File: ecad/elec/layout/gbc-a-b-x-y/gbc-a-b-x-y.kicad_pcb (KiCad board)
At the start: 2 copper layers, 225.7 x 100.8 mm, 0 parts

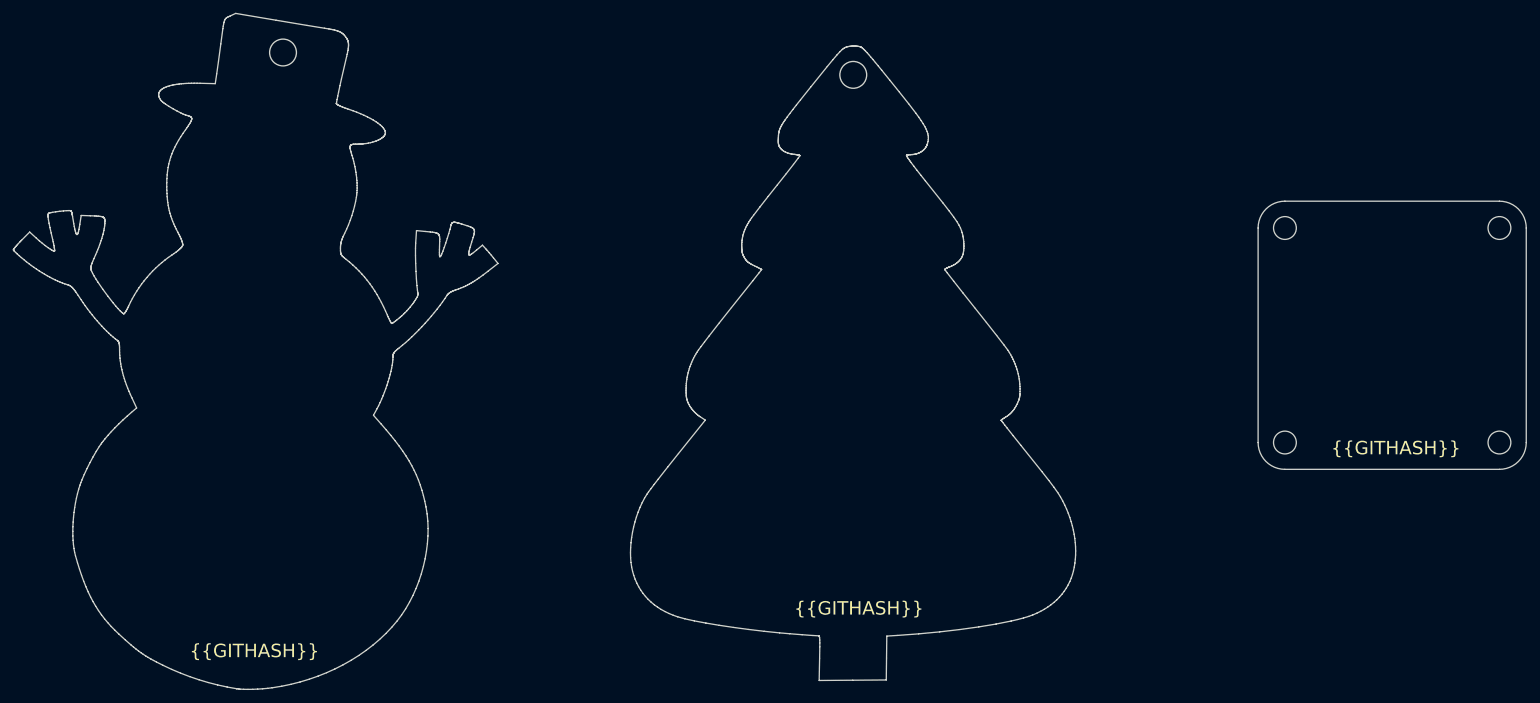
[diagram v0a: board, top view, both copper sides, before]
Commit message: WIP fleshing out and redoing some of the design to add some footprints / components for slik / membranes / etc.
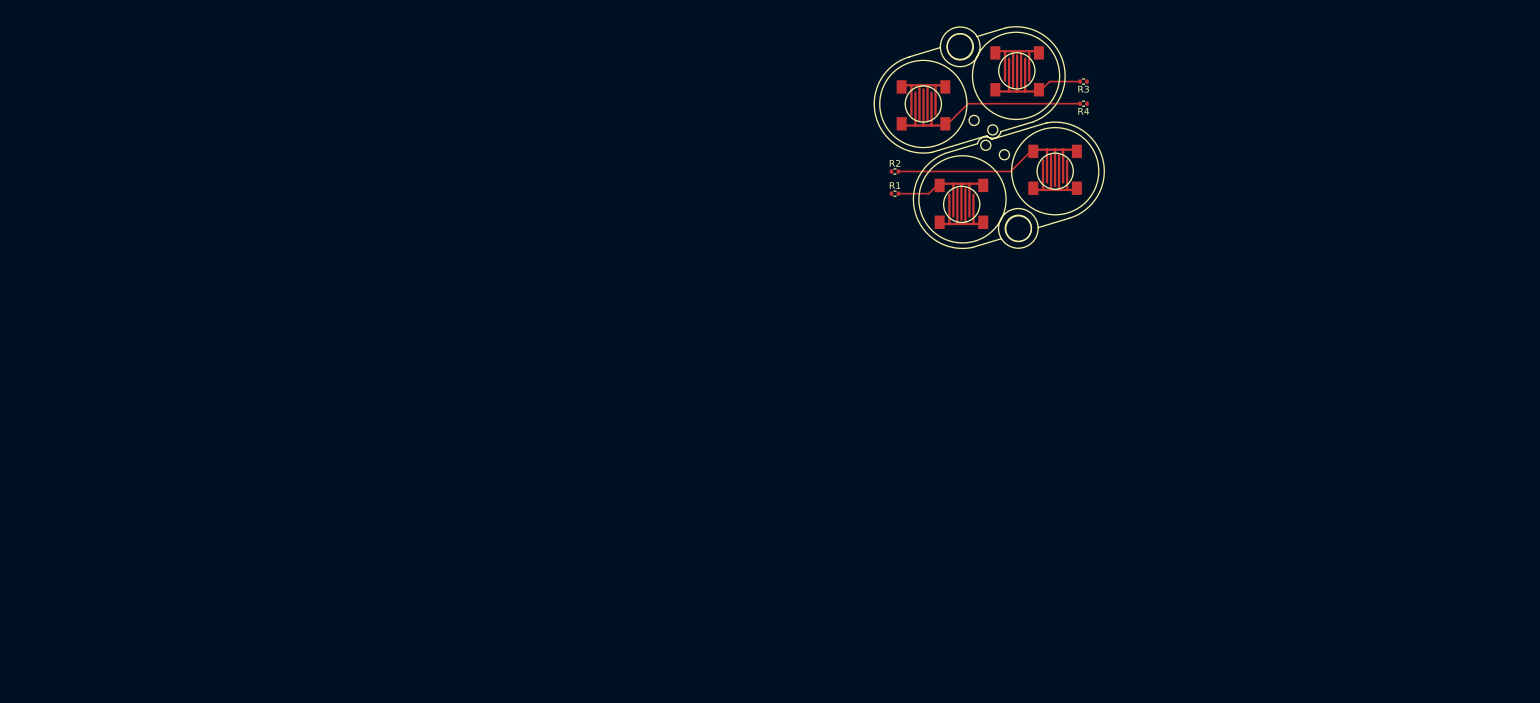
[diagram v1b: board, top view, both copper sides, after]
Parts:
- added R1: 62.5mW Thick Film Resistors 50V ±100ppm/℃ ±1% 10kΩ 0402 Chi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, lib:R0402, F.Cu at (167.5, 76.7)
- added R2: 62.5mW Thick Film Resistors 50V ±100ppm/℃ ±1% 10kΩ 0402 Chi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, lib:R0402, F.Cu at (167.5, 73.4)
- added R3: 62.5mW Thick Film Resistors 50V ±100ppm/℃ ±1% 10kΩ 0402 Chi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, lib:R0402, F.Cu at (195.6, 59.9)
- added R4: 62.5mW Thick Film Resistors 50V ±100ppm/℃ ±1% 10kΩ 0402 Chi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, lib:R0402, F.Cu at (195.6, 63.2)
- added U1: , lib:GAMEBOY_COLOR_A_B_BUTTON_MEMBRANE, F.Cu at (184.4, 75.8)
- added U2: , lib:GBC_A_B_BUTTON, F.Cu at (177.4, 78.2)
- added U3: , lib:GBC_A_B_BUTTON, F.Cu at (191.3, 73.1)
- added U4: , lib:GAMEBOY_COLOR_A_B_BUTTON_MEMBRANE, F.Cu at (178.7, 60.8)
- added U5: , lib:GBC_A_B_BUTTON, F.Cu at (185.7, 58.4)
- added U6: , lib:GBC_A_B_BUTTON, F.Cu at (171.7, 63.5)
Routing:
- net y: track 0.00 -> 21.0 mm
- net b: track 0.00 -> 21.0 mm
- net x: track 0.00 -> 6.28 mm
- net a: track 0.00 -> 6.28 mm
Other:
- board outline removed
- board text removed: "{{GITHASH}}"
